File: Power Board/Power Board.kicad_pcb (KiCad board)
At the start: 4 copper layers, 161 parts, among them IC1 LTC4151IMS#PBF, IC2 LTC4151IMS#PBF, J1 Conn_01x02, J18 Conn_02x03_Top_Bottom, J2 Conn_01x02, J3 Conn_01x02, J4 Conn_01x02, J5 Conn_01x02, J6 Conn_01x02, J7 Conn_01x02, J8 Conn_01x02, J9 Conn_02x03_Top_Bottom, Q1 Q_PMOS_GDS, Q10 Q_NMOS_GDS, Q11 Q_NMOS_GDS, Q12 Q_NMOS_GDS, Q13 Q_NMOS_GDS, Q14 Q_NMOS_GDS, Q15 Q_NMOS_GDS, Q16 Q_NMOS_GDS, Q17 Q_NMOS_GDS, Q18 Q_NMOS_GDS, Q19 Q_NMOS_GDS, Q2 Q_PMOS_GDS, Q20 Q_NMOS_GDS, Q21 Q_NMOS_GDS, Q22 Q_NMOS_GDS, Q3 Q_PMOS_GDS, Q4 Q_PMOS_GDS, Q5 Q_PMOS_GDS, Q6 Q_PMOS_GDS, Q7 Q_PMOS_GDS, Q8 Q_PMOS_GDS, Q9 Q_NMOS_GDS, U1 LTC4372CDD-PBF, U10 ACS770xCB-050U-PFF, U11 ACS770xCB-050U-PFF, U12 ACS770xCB-050U-PFF, U13 ACS770xCB-050U-PFF, U14 ACS770xCB-050U-PFF, U15 ADC128S052CIMT, U17 TLV70033_SOT23-5, U2 LTC4372CDD-PBF, U3 LTC4372CDD-PBF, U4 LTC4372CDD-PBF, U5 LTC4372CDD-PBF, U6 LTC4372CDD-PBF, U7 LTC4372CDD-PBF, U8 ACS770xCB-050U-PFF, U9 ACS770xCB-050U-PFF

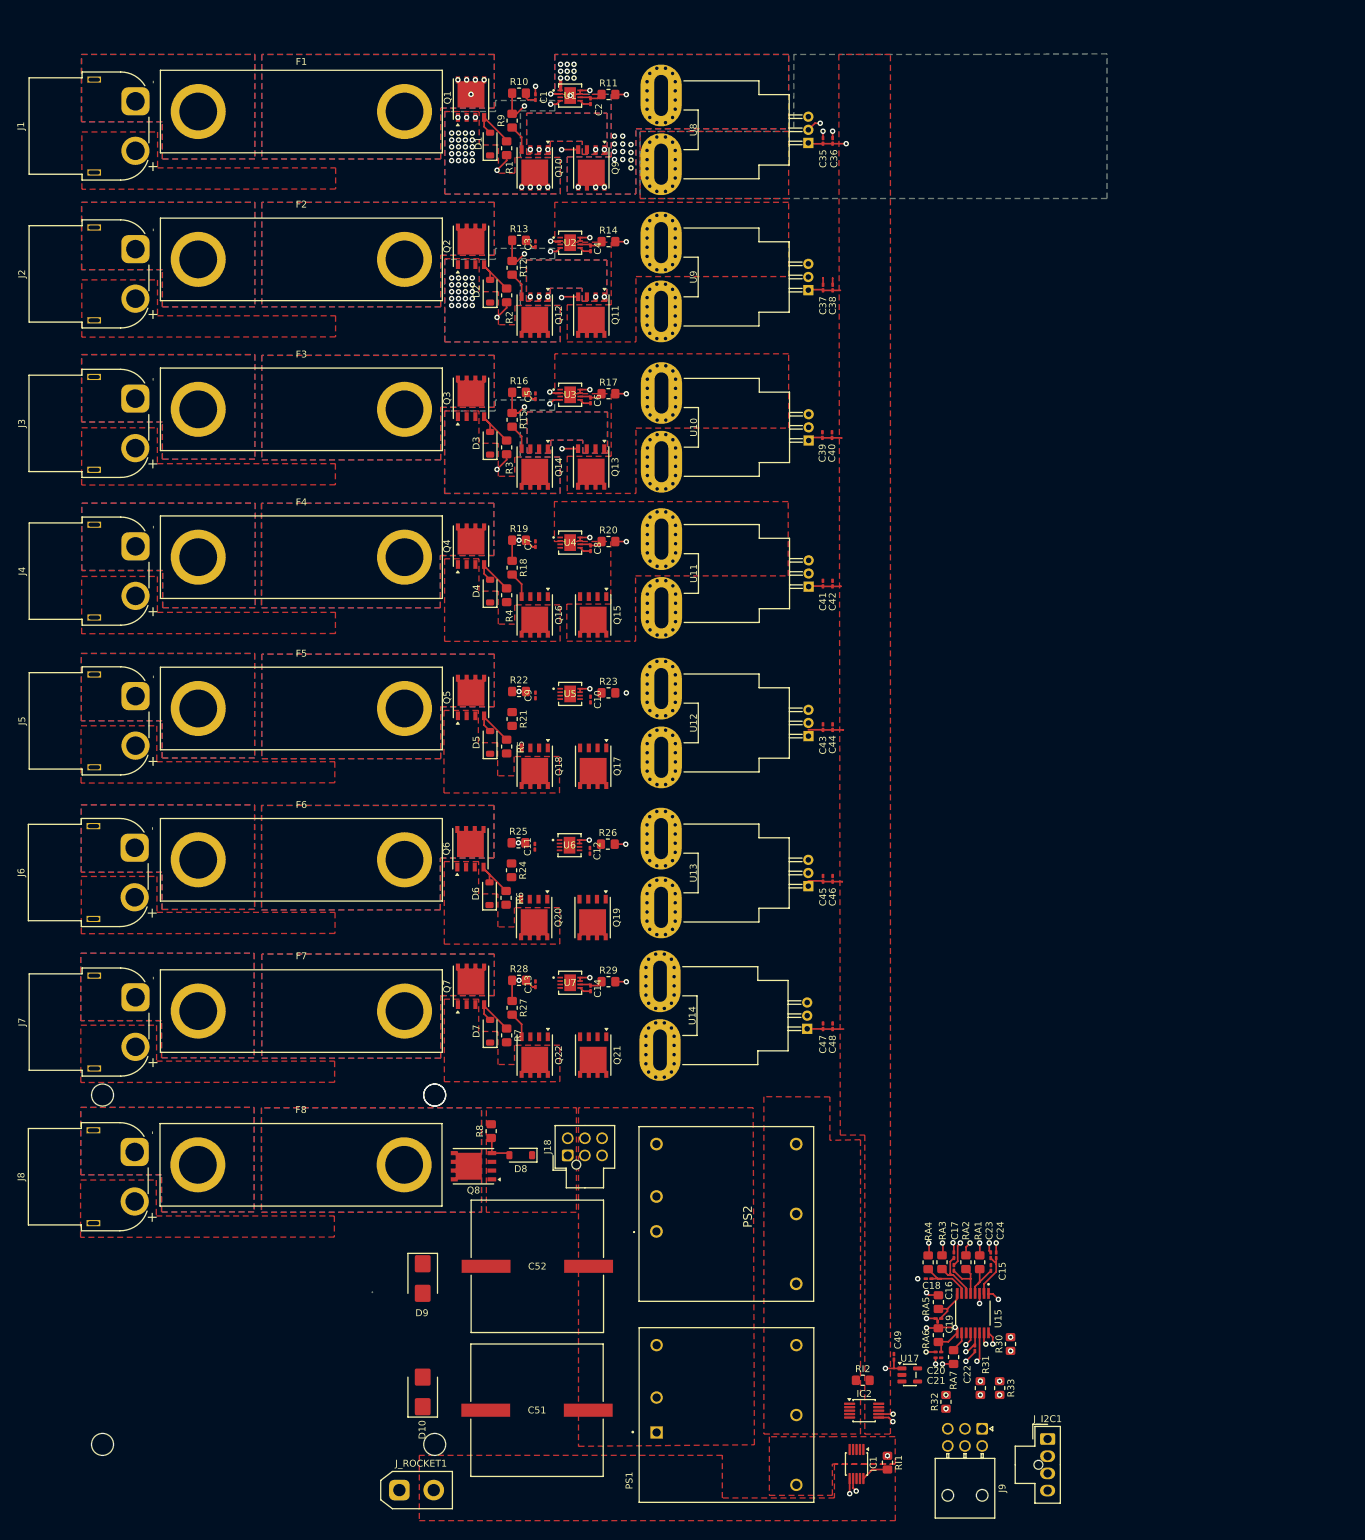
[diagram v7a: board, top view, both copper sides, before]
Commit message: added XT60 connectors for 5V rail and standoffs for BMS, 5V converter
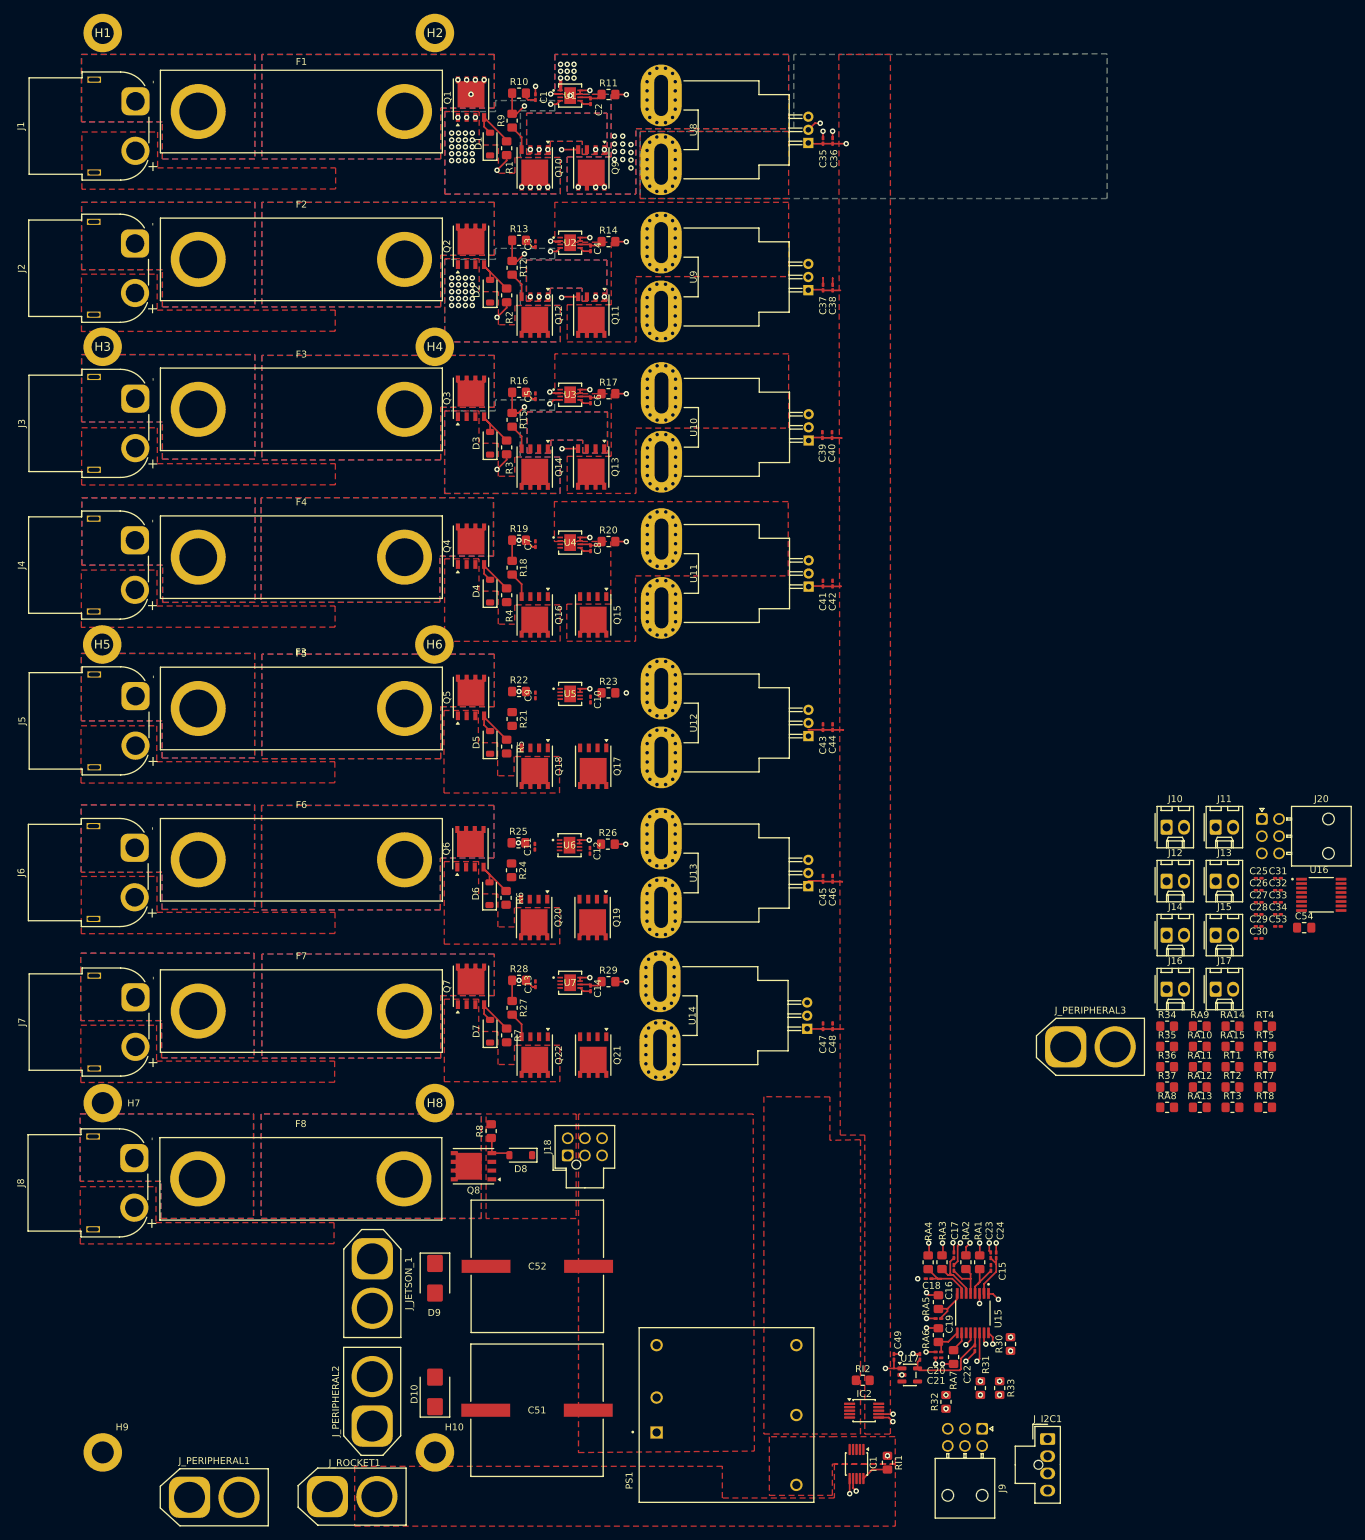
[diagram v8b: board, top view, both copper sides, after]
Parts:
- removed ? (x5): , 
- removed PS2: JTK3024S05, JTK3024S05:JTK3024S05
- added C25: 22 nF, Capacitor_SMD:C_0201_0603Metric_Pad0.64x0.40mm_HandSolder, F.Cu at (220.9, 148.0)
- added C26: 22 nF, Capacitor_SMD:C_0201_0603Metric_Pad0.64x0.40mm_HandSolder, F.Cu at (220.9, 149.7)
- added C27: 22 nF, Capacitor_SMD:C_0201_0603Metric_Pad0.64x0.40mm_HandSolder, F.Cu at (220.9, 151.5)
- added C28: 22 nF, Capacitor_SMD:C_0201_0603Metric_Pad0.64x0.40mm_HandSolder, F.Cu at (220.9, 153.2)
- added C29: 22 nF, Capacitor_SMD:C_0201_0603Metric_Pad0.64x0.40mm_HandSolder, F.Cu at (220.9, 155.0)
- added C30: 22 nF, Capacitor_SMD:C_0201_0603Metric_Pad0.64x0.40mm_HandSolder, F.Cu at (220.9, 156.7)
- added C31: 22 nF, Capacitor_SMD:C_0201_0603Metric_Pad0.64x0.40mm_HandSolder, F.Cu at (223.8, 148.0)
- added C32: 0.1 uF, Capacitor_SMD:C_0201_0603Metric_Pad0.64x0.40mm_HandSolder, F.Cu at (223.8, 149.7)
- added C33: 0.1 uF, Capacitor_SMD:C_0201_0603Metric_Pad0.64x0.40mm_HandSolder, F.Cu at (223.8, 151.5)
- added C34: 1 uF, Capacitor_SMD:C_0201_0603Metric_Pad0.64x0.40mm_HandSolder, F.Cu at (223.8, 153.2)
- added C53: 22 nF, Capacitor_SMD:C_0201_0603Metric_Pad0.64x0.40mm_HandSolder, F.Cu at (223.8, 155.0)
- added C54: 10uF, Capacitor_SMD:C_0805_2012Metric_Pad1.18x1.45mm_HandSolder, F.Cu at (227.6, 155.2)
- added H1: MountingHole_Pad, , F.Cu at (52.9, 25.1)
- added H10: MountingHole_Pad, MountingHole:MountingHole_3.2mm_M3_DIN965_Pad, F.Cu at (101.2, 231.5)
- added H2: MountingHole_Pad, , F.Cu at (101.2, 25.1)
- added H3: MountingHole_Pad, , F.Cu at (52.9, 70.7)
- added H4: MountingHole_Pad, , F.Cu at (101.2, 70.7)
- added H5: MountingHole_Pad, , F.Cu at (52.8, 114.0)
- added H6: MountingHole_Pad, , F.Cu at (101.1, 114.0)
- added H7: MountingHole_Pad, MountingHole:MountingHole_3.2mm_M3_DIN965_Pad, F.Cu at (52.9, 180.7)
- added H8: MountingHole_Pad, , F.Cu at (101.2, 180.7)
- added H9: MountingHole_Pad, MountingHole:MountingHole_3.2mm_M3_DIN965_Pad, F.Cu at (52.9, 231.5)
- added J10: Conn_01x02, Connector_Molex:Molex_KK-254_AE-6410-02A_1x02_P2.54mm_Vertical, F.Cu at (207.6, 140.6)
- added J11: Conn_01x02, Connector_Molex:Molex_KK-254_AE-6410-02A_1x02_P2.54mm_Vertical, F.Cu at (214.7, 140.6)
- added J12: Conn_01x02, Connector_Molex:Molex_KK-254_AE-6410-02A_1x02_P2.54mm_Vertical, F.Cu at (207.6, 148.4)
- added J13: Conn_01x02, Connector_Molex:Molex_KK-254_AE-6410-02A_1x02_P2.54mm_Vertical, F.Cu at (214.7, 148.4)
- added J14: Conn_01x02, Connector_Molex:Molex_KK-254_AE-6410-02A_1x02_P2.54mm_Vertical, F.Cu at (207.6, 156.3)
- added J15: Conn_01x02, Connector_Molex:Molex_KK-254_AE-6410-02A_1x02_P2.54mm_Vertical, F.Cu at (214.7, 156.3)
- added J16: Conn_01x02, Connector_Molex:Molex_KK-254_AE-6410-02A_1x02_P2.54mm_Vertical, F.Cu at (207.6, 164.1)
- added J17: Conn_01x02, Connector_Molex:Molex_KK-254_AE-6410-02A_1x02_P2.54mm_Vertical, F.Cu at (214.7, 164.1)
- added J20: Conn_02x03_Top_Bottom, Connector_Molex:Molex_Nano-Fit_105314-xx06_2x03_P2.50mm_Horizontal, F.Cu at (221.4, 139.4)
- added J_JETSON_1: Conn_01x02, Connector_AMASS:AMASS_XT60-F_1x02_P7.20mm_Vertical, F.Cu at (92.1, 203.3)
- added J_PERIPHERAL1: Conn_01x02, Connector_AMASS:AMASS_XT60-F_1x02_P7.20mm_Vertical, F.Cu at (65.5, 238.0)
- added J_PERIPHERAL2: Conn_01x02, Connector_AMASS:AMASS_XT60-F_1x02_P7.20mm_Vertical, F.Cu at (92.0, 227.6)
- added J_PERIPHERAL3: Conn_01x02, Connector_AMASS:AMASS_XT60-F_1x02_P7.20mm_Vertical, F.Cu at (192.9, 172.5)
- added R34: 33, Resistor_SMD:R_0805_2012Metric_Pad1.20x1.40mm_HandSolder, F.Cu at (207.6, 169.5)
- added R35: 33, Resistor_SMD:R_0805_2012Metric_Pad1.20x1.40mm_HandSolder, F.Cu at (207.6, 172.4)
- added R36: 33, Resistor_SMD:R_0805_2012Metric_Pad1.20x1.40mm_HandSolder, F.Cu at (207.6, 175.4)
- added R37: 33, Resistor_SMD:R_0805_2012Metric_Pad1.20x1.40mm_HandSolder, F.Cu at (207.6, 178.3)
- added RA10: 100, Resistor_SMD:R_0805_2012Metric_Pad1.20x1.40mm_HandSolder, F.Cu at (212.4, 172.4)
- added RA11: 100, Resistor_SMD:R_0805_2012Metric_Pad1.20x1.40mm_HandSolder, F.Cu at (212.4, 175.4)
- added RA12: 100, Resistor_SMD:R_0805_2012Metric_Pad1.20x1.40mm_HandSolder, F.Cu at (212.4, 178.3)
- added RA13: 100, Resistor_SMD:R_0805_2012Metric_Pad1.20x1.40mm_HandSolder, F.Cu at (212.4, 181.3)
- added RA14: 100, Resistor_SMD:R_0805_2012Metric_Pad1.20x1.40mm_HandSolder, F.Cu at (217.1, 169.5)
- added RA15: 100, Resistor_SMD:R_0805_2012Metric_Pad1.20x1.40mm_HandSolder, F.Cu at (217.1, 172.4)
- added RA8: 100, Resistor_SMD:R_0805_2012Metric_Pad1.20x1.40mm_HandSolder, F.Cu at (207.6, 181.3)
- added RA9: 100, Resistor_SMD:R_0805_2012Metric_Pad1.20x1.40mm_HandSolder, F.Cu at (212.4, 169.5)
- added RT1: 2.7K, Resistor_SMD:R_0805_2012Metric_Pad1.20x1.40mm_HandSolder, F.Cu at (217.1, 175.4)
- added RT2: 2.7K, Resistor_SMD:R_0805_2012Metric_Pad1.20x1.40mm_HandSolder, F.Cu at (217.1, 178.3)
- added RT3: 2.7K, Resistor_SMD:R_0805_2012Metric_Pad1.20x1.40mm_HandSolder, F.Cu at (217.1, 181.3)
- added RT4: 2.7K, Resistor_SMD:R_0805_2012Metric_Pad1.20x1.40mm_HandSolder, F.Cu at (221.9, 169.5)
- added RT5: 2.7K, Resistor_SMD:R_0805_2012Metric_Pad1.20x1.40mm_HandSolder, F.Cu at (221.9, 172.4)
- added RT6: 2.7K, Resistor_SMD:R_0805_2012Metric_Pad1.20x1.40mm_HandSolder, F.Cu at (221.9, 175.4)
- added RT7: 2.7K, Resistor_SMD:R_0805_2012Metric_Pad1.20x1.40mm_HandSolder, F.Cu at (221.9, 178.3)
- added RT8: 2.7K, Resistor_SMD:R_0805_2012Metric_Pad1.20x1.40mm_HandSolder, F.Cu at (221.9, 181.3)
- added U16: ADC128S052CIMT, ADC128S052CIMT_NOPB:SOP65P640X120-16N, F.Cu at (230.1, 150.4)
- J_ROCKET1: footprint Connector_AMASS:AMASS_XT30UPB-F_1x02_P5.0mm_Vertical -> Connector_AMASS:AMASS_XT60-F_1x02_P7.20mm_Vertical
- moved J_ROCKET1 10.5 mm to (85.5, 237.9)
- moved C50 5.37 mm to (171.7, 217.6)
- moved F8 2.04 mm to (81.7, 191.7)
- moved D9 1.79 mm to (101.2, 206.1)
- moved D10 1.79 mm to (101.2, 222.7)
- moved J8 0.90 mm to (57.5, 188.7)
- moved J4 0.89 mm to (57.5, 98.8)
- moved J2 0.82 mm to (57.6, 55.7)
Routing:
- net /3.3V: track 6.25 -> 14.1 mm, vias 2 -> 0
- net GND: track 38.1 -> 40.2 mm, vias 28 -> 31
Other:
- board text added: "F3"
